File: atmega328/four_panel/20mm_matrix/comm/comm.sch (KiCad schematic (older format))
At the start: 12 parts, among them IC5 ATMEGA328-A, P1 CONN15, P2 CONN15, P3 CONN_2X2, P4 CONN_2X2, X5 CER_RESO

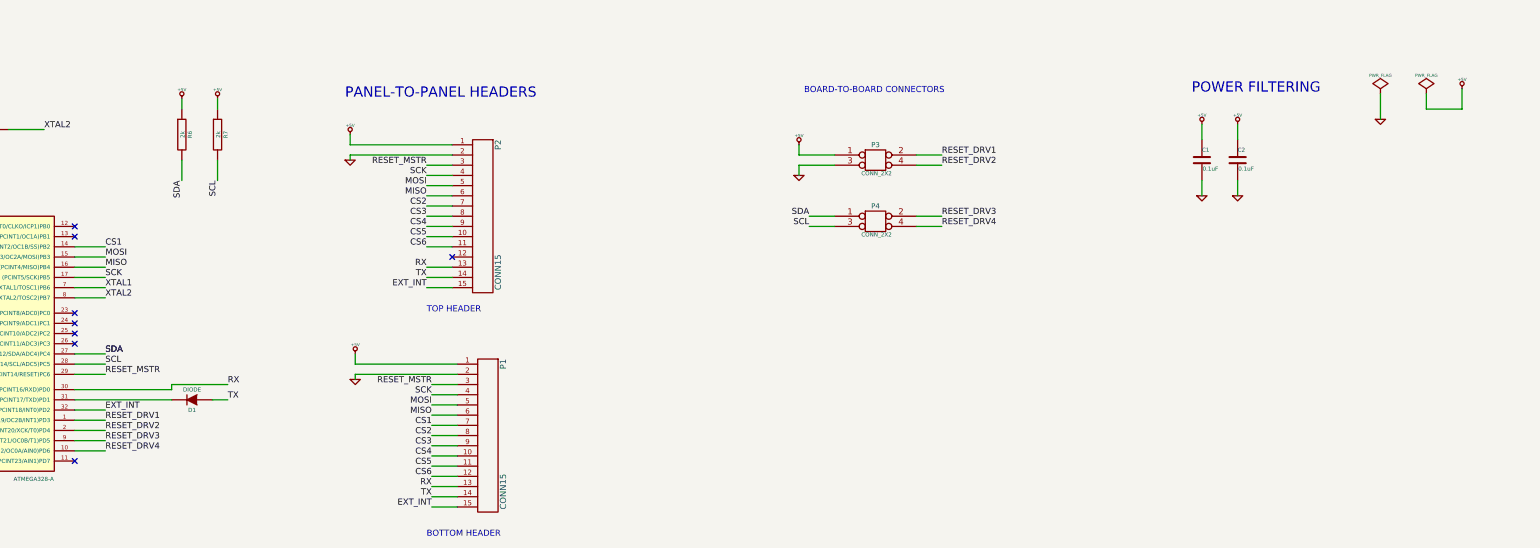
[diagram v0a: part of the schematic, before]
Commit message: Modified 4 matrix atmega328 design. Added pin change interrupts and re-routed.
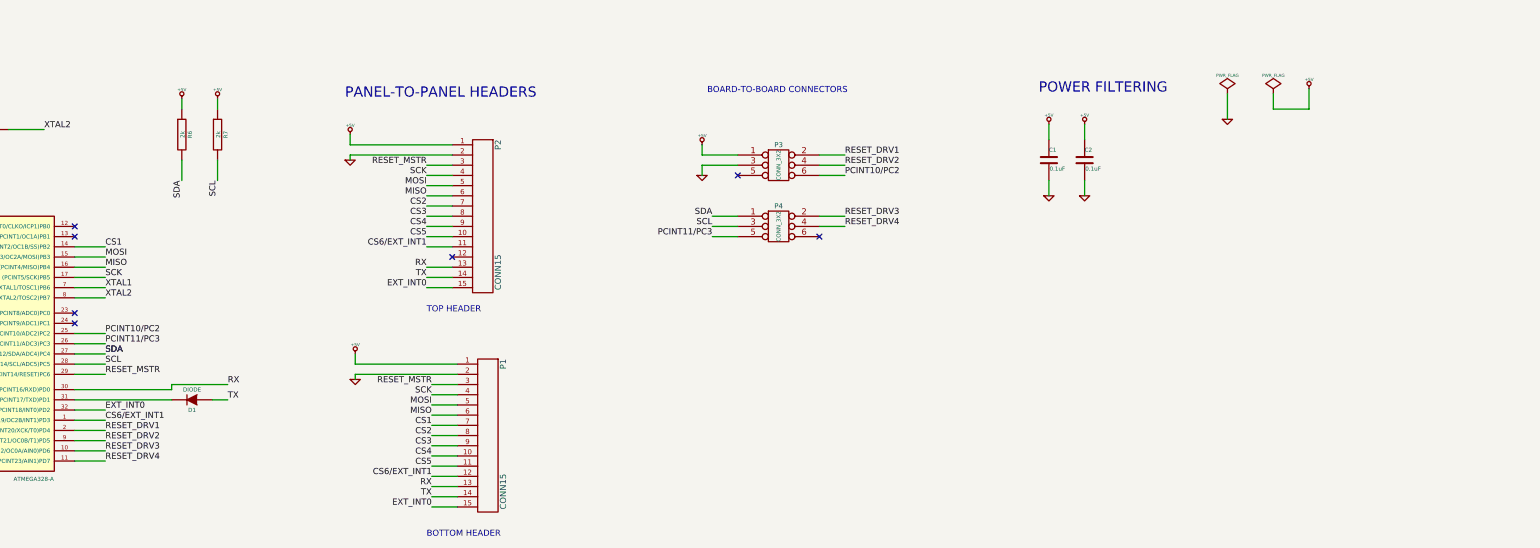
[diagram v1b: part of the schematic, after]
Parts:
- removed P3, P4: CONN_2X2, symbol CONN_2X2
- added P3, P4: CONN_3X2, symbol CONN_3X2
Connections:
- net +5V: now also P3.1
- net GND: now also P3.3
- net RESET_DRV1: now also IC5.2 ((PCINT20/XCK/T0)PD4), P3.2; no longer IC5.1 ((PCINT19/OC2B/INT1)PD3)
- net RESET_DRV2: now also IC5.9 ((PCINT21/OC0B/T1)PD5), P3.4; no longer IC5.2 ((PCINT20/XCK/T0)PD4)
- net RESET_DRV3: now also IC5.10 ((PCINT22/OC0A/AIN0)PD6), P4.2; no longer IC5.9 ((PCINT21/OC0B/T1)PD5)
- net RESET_DRV4: now also IC5.11 ((PCINT23/AIN1)PD7), P4.4; no longer IC5.10 ((PCINT22/OC0A/AIN0)PD6)
- net SCL: now also P4.3
- net SDA: now also P4.1
- net PCINT10/PC2: now reaches IC5.25 ((PCINT10/ADC2)PC2)
- net PCINT10/PC2: now also P3.6
- net PCINT11/PC3: now reaches IC5.26 ((PCINT11/ADC3)PC3)
- net PCINT11/PC3: now also P4.5
- net CS6 renamed CS6/EXT_INT1
- net CS6/EXT_INT1: now also IC5.1 ((PCINT19/OC2B/INT1)PD3)
- net EXT_INT renamed EXT_INT0
- no-connect marks 10 -> 9
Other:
- moved on the sheet: C1, C2
